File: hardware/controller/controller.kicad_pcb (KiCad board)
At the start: 4 copper layers, 100 x 80 mm, 66 parts, among them J1 USB_C_Receptacle_USB2.0_16P, J2 USB_C_Receptacle_USB2.0_16P, SW1 EVP-ASAC1A, SW2 CL-SB-13A-02T, SW3 EVP-ASAC1A, SW4 EVP-ASAC1A, SW5 EVP-ASAC1A, SW6 EVP-ASAC1A, U1 ZX-PM2.54-1-16PY, U10 XDJK-0051-025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

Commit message: updating symbols and board
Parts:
- J1, J2: value USB_C_Receptacle_USB2.0_16P -> TYPE-C 16PLT-H10.0; footprint footprints:TYPE-C-SMD_USB4120-03-C -> easyeda2kicad:TYPE-C-SMD_USB4120-03-C
- L1, L2, L3: footprint footprints:L0805 -> easyeda2kicad:L0805
- U7, U8, U9: footprint footprints:SOT-23-6_L2.9-W1.6-P0.95-LS2.8-BR -> easyeda2kicad:SOT-23-6_L2.9-W1.6-P0.95-LS2.8-BR
- moved U10 55.2 mm to (110.6, 139.6)
- moved J1 12.5 mm to (142.7, 114.9)
- moved J2 12.2 mm to (142.7, 121.3)
- moved C2 8.94 mm to (163.8, 88.7)
- moved C3 8.94 mm to (163.8, 90.6)
- moved C5 8.94 mm to (163.8, 92.6)
- moved R10 8.94 mm to (142.8, 95.5)
- moved R21 8.94 mm to (169.6, 82.7)
- moved R22 8.94 mm to (169.6, 84.7)
- moved R23 8.94 mm to (169.6, 86.7)
- moved R5 8.94 mm to (142.8, 83.0)
- moved R6 8.94 mm to (142.8, 85.5)
- moved R7 8.94 mm to (142.8, 88.0)
- moved R8 8.94 mm to (142.8, 90.5)
- moved R9 8.94 mm to (142.8, 93.0)
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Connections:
- J1 pad 0: (no net) -> GND
- J2 pad 0: (no net) -> GND
- R12 pad 1: GND -> Net-(J1-CC2)
- R12 pad 2: Net-(J1-CC2) -> GND
- R13 pad 1: GND -> Net-(J2-CC2)
- R13 pad 2: Net-(J2-CC1) -> GND
- R14 pad 2: Net-(J2-CC2) -> Net-(J2-CC1)

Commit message: moving some more things around
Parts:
- moved R21 148.1 mm to (46.2, 164.6)
- moved R22 148.1 mm to (46.2, 166.6)
- moved C17 145.3 mm to (42.2, 162.7)
- moved R23 145.2 mm to (45.6, 162.2)
- moved L3 126.9 mm to (50.8, 158.2)
- moved C19 126.9 mm to (42.0, 165.1)
- moved C20 126.9 mm to (42.0, 167.6)
- moved R19 123.8 mm to (68.6, 160.3)
- moved C11 123.6 mm to (72.7, 165.5)
- moved R15 120.6 mm to (75.9, 165.2)
- moved C12 116.1 mm to (63.8, 138.7)
- moved R20 115.5 mm to (60.1, 131.1)
- moved R17 115.4 mm to (79.2, 165.1)
- moved R18 113.8 mm to (67.5, 138.4)
- moved R16 107.8 mm to (68.5, 135.1)
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
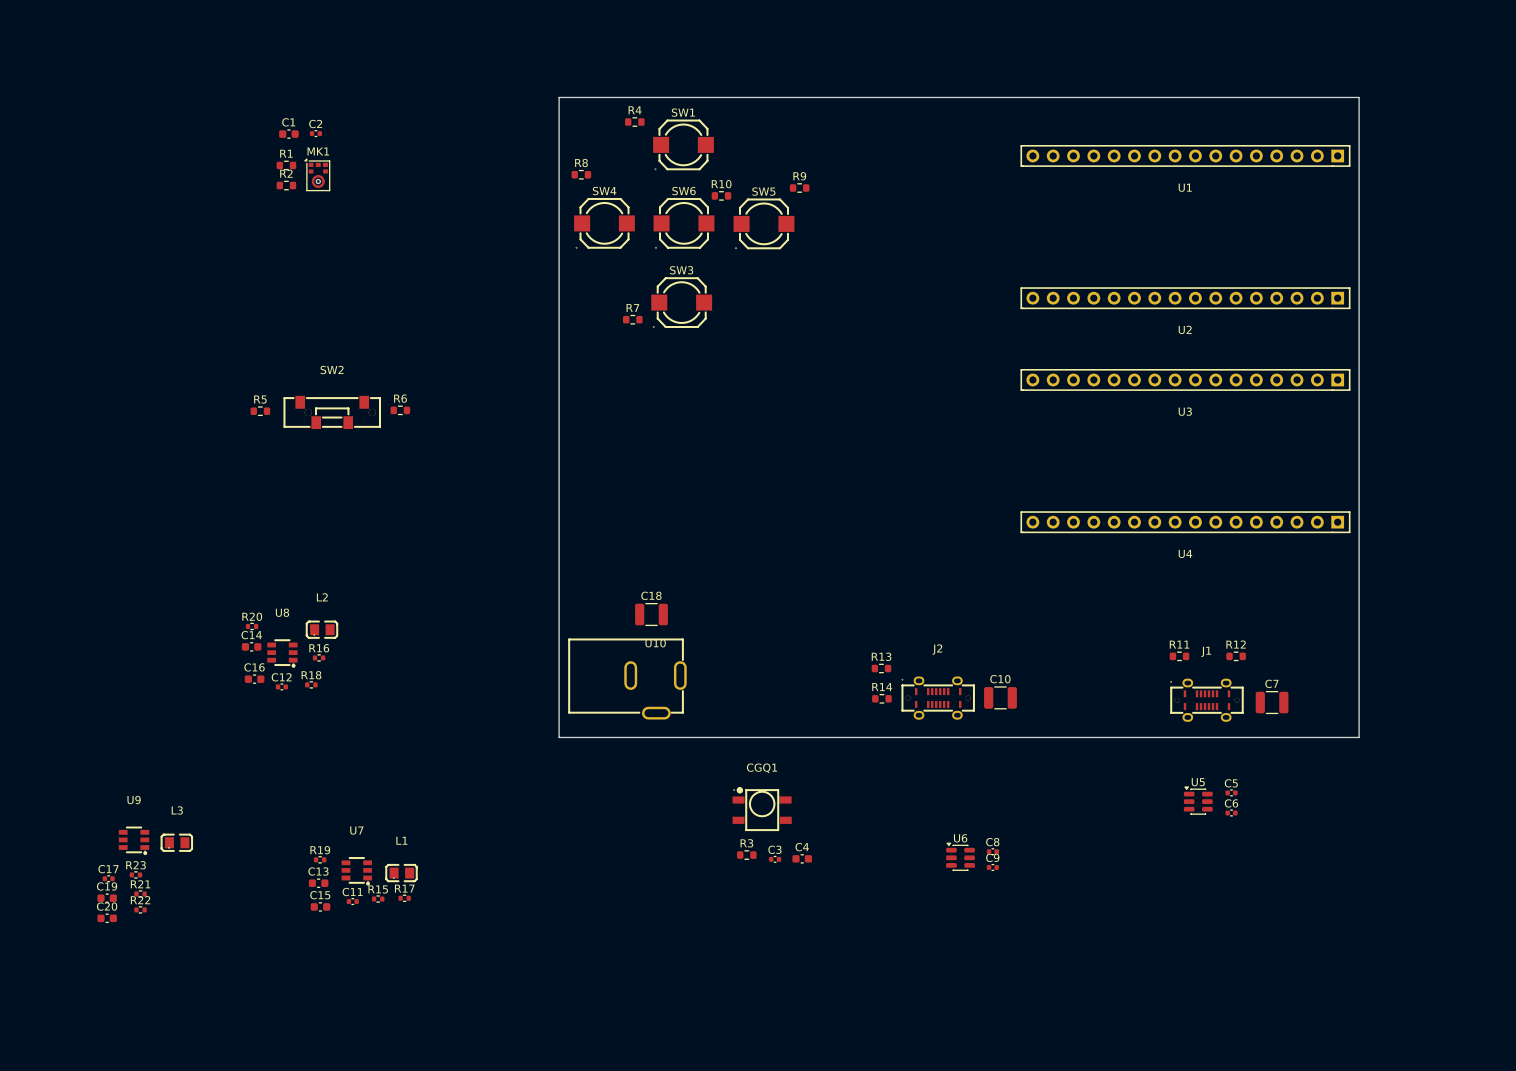
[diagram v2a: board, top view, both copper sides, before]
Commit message: rotate/move around items on controller board
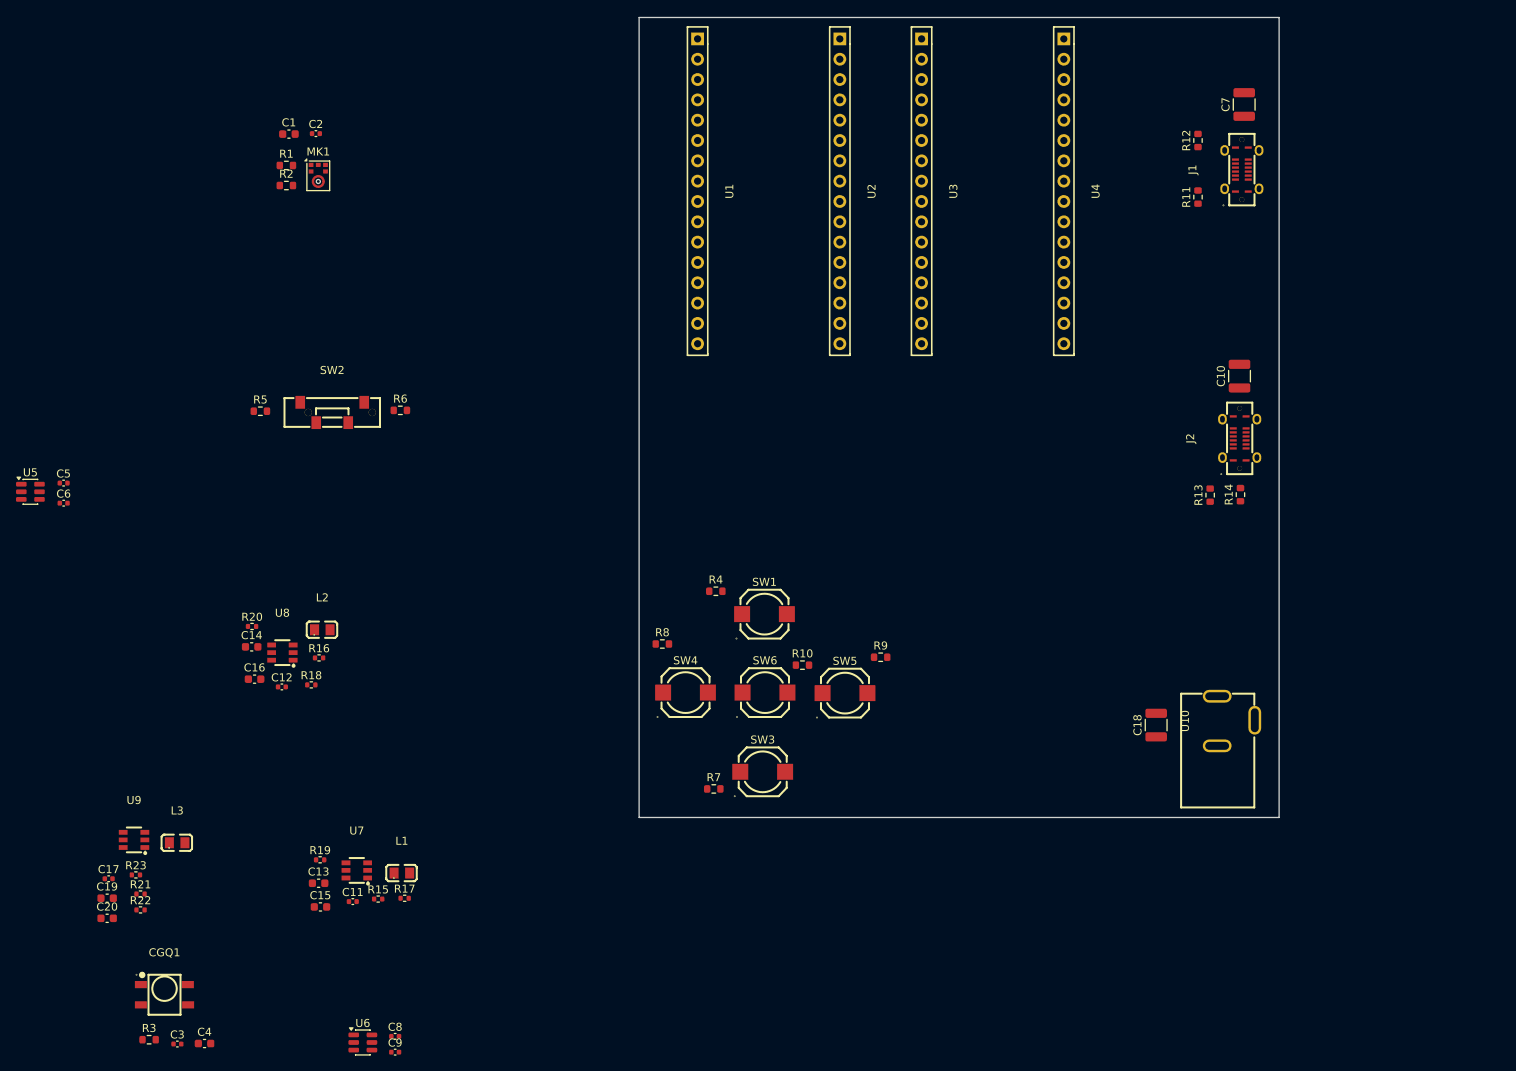
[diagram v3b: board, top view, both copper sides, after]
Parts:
- moved C5 151.0 mm to (36.6, 113.2)
- moved U5 151.0 mm to (32.4, 114.3)
- moved C6 151.0 mm to (36.6, 115.7)
- moved C4 78.2 mm to (54.2, 183.3)
- moved C3 78.2 mm to (50.8, 183.3)
- moved CGQ1 78.2 mm to (49.2, 177.2)
- moved R3 78.2 mm to (47.2, 182.8)
- moved U6 78.2 mm to (74.0, 183.1)
- moved C8 78.2 mm to (78.0, 182.4)
- moved C9 78.2 mm to (78.0, 184.3)
- moved C7 74.8 mm to (184.1, 65.9), turned to 90 degrees
- moved U10 72.6 mm to (183.1, 142.9), turned to 90 degrees
- moved J1 66.5 mm to (183.8, 74.0), turned to 90 degrees
- moved R12 64.7 mm to (178.4, 70.4), turned to 90 degrees
- moved C18 64.6 mm to (173.1, 143.4), turned to 90 degrees
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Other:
- board size 100 x 80 mm -> 80 x 100 mm

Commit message: adding some more stuff
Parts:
- added H1: MountingHole, MountingHole:MountingHole_3.2mm_M3_Pad, F.Cu at (113.5, 150.0)
- added H2: MountingHole, MountingHole:MountingHole_3.2mm_M3_Pad, F.Cu at (183.5, 60.0)
- added H3: MountingHole, MountingHole:MountingHole_3.2mm_M3_Pad, F.Cu at (113.5, 60.0)
- added H4: MountingHole, MountingHole:MountingHole_3.2mm_M3_Pad, F.Cu at (183.5, 150.0)
- moved R1 114.9 mm to (178.1, 90.0), turned to 180 degrees
- moved C1 112.1 mm to (175.9, 84.0), turned to 90 degrees
- moved MK1 109.9 mm to (177.6, 87.4), turned to 90 degrees
- moved R2 109.8 mm to (173.6, 87.4)
- moved C2 107.4 mm to (174.5, 84.5), turned to 90 degrees
- moved C7 67.8 mm to (175.5, 133.1), turned to -90 degrees
- moved R11 60.0 mm to (183.6, 137.3)
- moved J1 58.8 mm to (182.2, 132.8), turned to 180 degrees
- moved R12 57.9 mm to (181.2, 128.2)
- moved C10 44.8 mm to (153.1, 132.7), turned to -90 degrees
- moved J2 34.3 mm to (159.9, 132.5), turned to 180 degrees
- moved R14 31.8 mm to (160.9, 136.7)
- moved R13 24.9 mm to (159.0, 128.3)
- moved C18 14.5 mm to (159.1, 147.3)
- moved U10 14.5 mm to (169.1, 146.8)
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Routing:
- added copper zone on In1.Cu, net GND

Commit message: controller layout work
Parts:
- moved R22 170.6 mm to (211.2, 123.1)
- moved R21 169.8 mm to (211.2, 124.3)
- moved C17 169.2 mm to (207.8, 128.0)
- moved C20 167.0 mm to (203.3, 124.3)
- moved U9 165.7 mm to (207.8, 125.3)
- moved R23 165.4 mm to (206.2, 122.3), turned to 90 degrees
- moved C19 165.3 mm to (203.3, 129.0)
- moved L3 155.5 mm to (203.0, 126.5), turned to 180 degrees
- moved C11 145.1 mm to (207.9, 112.8)
- moved C13 145.1 mm to (203.7, 110.5)
- moved C15 145.1 mm to (203.9, 113.4)
- moved L1 145.1 mm to (214.1, 109.2)
- moved R15 145.1 mm to (211.1, 112.5)
- moved R17 145.1 mm to (214.4, 112.4)
- moved R19 145.1 mm to (203.9, 107.5)
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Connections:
- C1 pad 1: SOUND REACTIVE OFF -> +3.3V
- C19 pad 1: SOUND REACTIVE OFF -> +3.3V
- C2 pad 1: SOUND REACTIVE OFF -> +3.3V
- C6 pad 2: SOUND REACTIVE OFF -> +3.3V
- C9 pad 2: SOUND REACTIVE OFF -> +3.3V
- L3 pad 2: SOUND REACTIVE OFF -> +3.3V
- MK1 pad 5: SOUND REACTIVE OFF -> +3.3V
- R10 pad 1: SOUND REACTIVE OFF -> +3.3V
- R22 pad 2: SOUND REACTIVE OFF -> +3.3V
- R3 pad 2: SOUND REACTIVE OFF -> +3.3V
- R4 pad 1: SOUND REACTIVE OFF -> +3.3V
- R5 pad 1: SOUND REACTIVE OFF -> SOUND REACTIVE ON
- R7 pad 1: SOUND REACTIVE OFF -> +3.3V
- R8 pad 1: SOUND REACTIVE OFF -> +3.3V
- R9 pad 1: SOUND REACTIVE OFF -> +3.3V
- SW2 pad 1: SOUND REACTIVE OFF -> SOUND REACTIVE ON
- SW2 pad 3: GND -> +3.3V
- U1 pad 10: SOUND REACTIVE OFF -> SOUND REACTIVE ON
- U5 pad 6: SOUND REACTIVE OFF -> +3.3V
- U6 pad 6: SOUND REACTIVE OFF -> +3.3V
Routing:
- net GND: track 0.00 -> 56.6 mm, vias 0 -> 17
- net +12V: track 0.00 -> 25.2 mm, vias 0 -> 7
- net +3.3V: track 0.00 -> 6.57 mm
- net +4V: track 0.00 -> 5.49 mm
- net Net-(U8-SWITCH): track 0.00 -> 4.18 mm
- net Net-(J2-CC1): track 0.00 -> 3.30 mm
- net Net-(J2-CC2): track 0.00 -> 3.26 mm
- net SHIFTED_LED_DATA_2: track 0.00 -> 3.20 mm
- net SHIFTED_LED_DATA_1: track 0.00 -> 3.20 mm
- net Net-(J1-CC2): track 0.00 -> 3.17 mm
- net Net-(J1-CC1): track 0.00 -> 3.14 mm
- net Net-(U8-FBK): track 0.00 -> 2.87 mm
- net SOUND REACTIVE OFF: track 0.00 -> 1.82 mm
- net Net-(U8-BOOT): track 0.00 -> 1.77 mm
- net SOUND REACTIVE ON: track 0.00 -> 1.77 mm
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- added copper zone on In2.Cu, net +12V

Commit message: placement and initial routing
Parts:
- moved R17 76.0 mm to (150.3, 153.0), turned to 180 degrees
- moved L1 75.5 mm to (148.1, 145.7), turned to 180 degrees
- moved U7 71.1 mm to (149.8, 149.1), turned to -90 degrees
- moved C11 70.6 mm to (147.4, 149.1), turned to 90 degrees
- moved R15 70.5 mm to (152.5, 151.5)
- moved R19 65.1 mm to (152.5, 147.6)
- moved C13 64.8 mm to (147.9, 143.6)
- moved R22 62.9 mm to (148.6, 129.1), turned to 180 degrees
- moved C17 60.9 mm to (147.0, 125.3), turned to 90 degrees
- moved R21 60.8 mm to (150.5, 128.7), turned to -90 degrees
- moved C15 60.0 mm to (152.9, 145.1), turned to 90 degrees
- moved U9 58.2 mm to (149.6, 125.4), turned to -90 degrees
- moved C19 58.0 mm to (145.9, 120.8), turned to -90 degrees
- moved L3 55.0 mm to (148.3, 120.5), turned to 90 degrees
- moved R23 53.7 mm to (152.5, 123.7), turned to 0 degrees
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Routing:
- net EAR TO EYE AUDIO: track 0.00 -> 133.1 mm, vias 0 -> 1
- net BTN LEFT: track 0.00 -> 74.7 mm, vias 0 -> 1
- net LED DATA_2: track 1.43 -> 70.6 mm, vias 1 -> 3
- net BTN DOWN: track 0.00 -> 67.6 mm, vias 0 -> 1
- net IR SENSOR DATA: track 0.00 -> 60.4 mm, vias 0 -> 1
- net LED DATA_1: track 1.45 -> 56.9 mm, vias 1 -> 0
- net BTN RIGHT: track 0.00 -> 51.3 mm
- net BTN UP: track 0.00 -> 49.8 mm, vias 0 -> 1
- net BTN CENTER: track 0.00 -> 48.5 mm
- net SHIFTED_LED_DATA_2: track 3.20 -> 41.4 mm, vias 0 -> 2
- net GND: track 56.6 -> 89.2 mm, vias 17 -> 35
- net SOUND REACTIVE OFF: track 1.82 -> 29.1 mm, vias 0 -> 1
- net SHIFTED_LED_DATA_1: track 3.20 -> 28.6 mm, vias 0 -> 2
- net MIC DATA OUTPUT: track 1.74 -> 24.8 mm, vias 0 -> 1
- net SOUND REACTIVE ON: track 1.77 -> 24.6 mm
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- added copper zone on In2.Cu, net +3.3V
- added copper zone on In2.Cu, net +4V
- added copper zone on In2.Cu, net +5V
